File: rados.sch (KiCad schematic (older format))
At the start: 1 part

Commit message: More routing
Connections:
- net labels added: AUX-1, AUX-2, AUX-3, AUX-4, LCD-D4, LCD-D5, LCD-D6, LCD-D7, Probe
- net labels removed: LCD-4, LCD-5, LCD-6, LCD-7
- wire segments 66 -> 75
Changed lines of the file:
@@
 Text GLabel 5100 2800 2    47   Output ~ 0
 HP-FET2
-Text GLabel 5100 2700 2    47   Output ~ 0
+Text GLabel 5100 3400 2    47   Output ~ 0
 HP-FET3
+Text GLabel 5125 3700 2    47   Output ~ 0
+MP-FET1
+Text GLabel 5125 3800 2    47   Output ~ 0
+LP-FET1
 Text GLabel 5125 3900 2    47   Output ~ 0
-MP-FET1
-Text GLabel 5125 4100 2    47   Output ~ 0
-LP-FET1
-Text GLabel 5125 4000 2    47   Output ~ 0
 LP-FET2
 Wire Wire Line
@@
 	5000 2500 5100 2500
 Wire Wire Line
-	5000 2700 5100 2700
+	5000 3400 5100 3400
 Wire Wire Line
 	5100 2800 5000 2800
@@
 Text GLabel 5100 2100 2    47   Output ~ 0
 Z-EN
-Text GLabel 5125 3800 2    47   Output ~ 0
+Text GLabel 5100 3200 2    47   Output ~ 0
 Y-DIR
-Text GLabel 5125 3400 2    47   Output ~ 0
+Text GLabel 5100 3300 2    47   Output ~ 0
 Y-STEP
 Text GLabel 5125 4200 2    47   BiDi ~ 0
@@
 Wire Wire Line
 	5000 4625 5000 4725
-Text GLabel 5125 5050 2    47   Output ~ 0
+Text GLabel 5100 3100 2    47   Output ~ 0
 Y-EN
-Text GLabel 5125 5150 2    47   Output ~ 0
+Text GLabel 5125 4100 2    47   Output ~ 0
 X-DIR
-Text GLabel 5125 5250 2    47   Output ~ 0
+Text GLabel 5125 4000 2    47   Output ~ 0
 X-STEP
-Text GLabel 5125 5450 2    47   Output ~ 0
+Text GLabel 3000 6400 0    47   Output ~ 0
 X-EN
-Text GLabel 5125 5650 2    47   Input ~ 0
+Text GLabel 5125 5050 2    47   Input ~ 0
 X-
-Text GLabel 5125 5900 2    47   Input ~ 0
+Text GLabel 5125 5250 2    47   Input ~ 0
 Y-
-Text GLabel 5125 6100 2    47   Input ~ 0
+Text GLabel 5125 5450 2    47   Input ~ 0
 Z-
-Text GLabel 5125 6300 2    47   Input ~ 0
+Text GLabel 5125 5150 2    47   Input ~ 0
 X+
-Text GLabel 5125 6500 2    47   Input ~ 0
+Text GLabel 5125 5350 2    47   Input ~ 0
 Y+
-Text GLabel 3000 6600 0    47   Input ~ 0
+Text GLabel 5125 5550 2    47   Input ~ 0
 Z+
 Wire Wire Line
-	5000 5050 5125 5050
+	5125 5050 5000 5050
+Wire Wire Line
+	5000 5250 5125 5250
+Wire Wire Line
+	5000 5450 5125 5450
 Wire Wire Line
 	5125 5150 5000 5150
 Wire Wire Line
-	5000 5250 5125 5250
-Wire Wire Line
-	5000 5450 5125 5450
+	5000 5550 5125 5550
+Wire Wire Line
+	5125 6000 5000 6000
+Wire Wire Line
+	5000 5350 5125 5350
 Wire Wire Line
 	5125 5650 5000 5650
 Wire Wire Line
-	5000 5900 5125 5900
-Wire Wire Line
-	5125 6100 5000 6100
-Wire Wire Line
-	5000 6300 5125 6300
-Wire Wire Line
-	5125 6500 5000 6500
-Wire Wire Line
-	3000 6600 3100 6600
-Text GLabel 3000 6150 0    47   BiDi ~ 0
+	5125 6200 5000 6200
+Text GLabel 3000 6600 0    47   BiDi ~ 0
 LCD-RS
-Text GLabel 3000 6050 0    47   BiDi ~ 0
+Text GLabel 5125 6500 2    47   BiDi ~ 0
 LCD-E
-Text GLabel 3000 5950 0    47   BiDi ~ 0
-LCD-4
-Text GLabel 3000 5850 0    47   BiDi ~ 0
-LCD-5
-Text GLabel 3000 5750 0    47   BiDi ~ 0
-LCD-6
-Text GLabel 3000 5650 0    47   BiDi ~ 0
-LCD-7
-Text GLabel 3000 5550 0    47   BiDi ~ 0
+Text GLabel 5125 6200 2    47   BiDi ~ 0
+LCD-D4
+Text GLabel 5125 6600 2    47   BiDi ~ 0
+LCD-D5
+Text GLabel 5125 6400 2    47   BiDi ~ 0
+LCD-D6
+Text GLabel 5125 6300 2    47   BiDi ~ 0
+LCD-D7
+Text GLabel 2975 5550 0    47   BiDi ~ 0
 ENC-SW
-Text GLabel 3000 5300 0    47   BiDi ~ 0
+Text GLabel 3000 6500 0    47   BiDi ~ 0
 ENC-B
-Text GLabel 3000 5100 0    47   BiDi ~ 0
+Text GLabel 3000 6300 0    47   BiDi ~ 0
 ENC-A
 Wire Wire Line
-	3000 6150 3100 6150
-Wire Wire Line
-	3100 6050 3000 6050
-Wire Wire Line
-	3000 5950 3100 5950
-Wire Wire Line
-	3100 5850 3000 5850
-Wire Wire Line
-	3000 5750 3100 5750
-Wire Wire Line
-	3100 5650 3000 5650
-Wire Wire Line
-	3000 5550 3100 5550
+	2975 5550 3100 5550
 Wire Wire Line
 	3000 5300 3100 5300
 Wire Wire Line
 	3100 5100 3000 5100
-Text GLabel 3000 5450 0    47   Output ~ 0
+Text GLabel 2975 6150 0    47   Output ~ 0
 E3-EN
-Text GLabel 3000 5200 0    47   Output ~ 0
+Text GLabel 2975 5950 0    47   Output ~ 0
 E3-STEP
-Text GLabel 3000 5000 0    47   Output ~ 0
+Text GLabel 2975 5750 0    47   Output ~ 0
 E3-DIR
 Wire Wire Line
@@
 Wire Wire Line
 	3100 4625 3100 4850
-Text GLabel 3000 4000 0    47   Output ~ 0
+Text GLabel 2975 3300 0    47   Output ~ 0
 E2-STEP
-Text GLabel 3000 3400 0    47   Output ~ 0
+Text GLabel 2975 3400 0    47   Output ~ 0
 E2-EN
-Text GLabel 3000 3900 0    47   Output ~ 0
+Text GLabel 2975 3200 0    47   Output ~ 0
 E2-DIR
 Wire Wire Line
-	3000 3400 3100 3400
+	2975 3400 3100 3400
 Wire Wire Line
 	3100 4000 3000 4000
 Wire Wire Line
 	3000 3900 3100 3900
-Text GLabel 3000 3600 0    47   Output ~ 0
+Text GLabel 2975 3000 0    47   Output ~ 0
 E1-STEP
-Text GLabel 3000 3800 0    47   Output ~ 0
+Text GLabel 2975 3100 0    47   Output ~ 0
 E1-EN
-Text GLabel 3000 3500 0    47   Output ~ 0
+Text GLabel 2975 2900 0    47   Output ~ 0
 E1-DIR
 Wire Wire Line
@@
 Wire Wire Line
 	3000 2200 3100 2200
-Text GLabel 3000 4500 0    47   Input ~ 0
+Text GLabel 3000 4100 0    47   Input ~ 0
 T0
-Text GLabel 3000 4400 0    47   Input ~ 0
+Text GLabel 3000 4200 0    47   Input ~ 0
 T1
 Text GLabel 3000 4300 0    47   Input ~ 0
 T2
-Text GLabel 3000 4200 0    47   Input ~ 0
+Text GLabel 3000 4400 0    47   Input ~ 0
 T3
-Text GLabel 3000 4100 0    47   Input ~ 0
+Text GLabel 3000 4500 0    47   Input ~ 0
 T4
 Wire Wire Line
@@
 Wire Wire Line
 	3000 4100 3100 4100
-Text GLabel 3000 6300 0    47   Input ~ 0
+Text GLabel 5125 5750 2    47   Input ~ 0
 STATUS-LED
 Wire Wire Line
@@
 	5000 4000 5125 4000
 Wire Wire Line
-	5125 3400 5000 3400
+	5100 3300 5000 3300
+Text GLabel 5125 5650 2    47   Input ~ 0
+Probe
+Wire Wire Line
+	5000 6400 5125 6400
+Wire Wire Line
+	5000 6500 5125 6500
+Wire Wire Line
+	3000 6400 3100 6400
+Wire Wire Line
+	3000 6600 3100 6600
+Wire Wire Line
+	5125 6600 5000 6600
+Wire Wire Line
+	5125 6300 5000 6300
+Text GLabel 3000 3600 0    47   BiDi ~ 0
+AUX-1
+Text GLabel 3000 3800 0    47   BiDi ~ 0
+AUX-2
+Text GLabel 3000 3900 0    47   BiDi ~ 0
+AUX-3
+Text GLabel 3000 4000 0    47   BiDi ~ 0
+AUX-4
+Wire Wire Line
+	2975 2900 3100 2900
+Wire Wire Line
+	3100 3000 2975 3000
+Wire Wire Line
+	2975 3100 3100 3100
+Wire Wire Line
+	2975 3200 3100 3200
+Wire Wire Line
+	3100 3300 2975 3300
+Wire Wire Line
+	3000 6500 3100 6500
+Wire Wire Line
+	3100 6150 2975 6150
+Wire Wire Line
+	5125 5750 5000 5750
+Wire Wire Line
+	2975 5750 3100 5750
+Wire Wire Line
+	2975 5950 3100 5950
 $EndSCHEMATC

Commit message: Routing almost finished
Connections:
- wire segments 75 -> 77
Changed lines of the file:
@@
 Text GLabel 5100 2000 2    47   Output ~ 0
 HB-FET
-Text GLabel 5100 2500 2    47   Output ~ 0
+Text GLabel 5100 2700 2    47   Output ~ 0
 HP-FET1
 Text GLabel 5100 2800 2    47   Output ~ 0
@@
 Text GLabel 5100 2200 2    47   Output ~ 0
 Z-DIR
-Text GLabel 5100 2400 2    47   Output ~ 0
+Text GLabel 5100 2500 2    47   Output ~ 0
 Z-STEP
 Wire Wire Line
@@
 Text GLabel 5100 3200 2    47   Output ~ 0
 Y-DIR
-Text GLabel 5100 3300 2    47   Output ~ 0
+Text GLabel 5100 3100 2    47   Output ~ 0
 Y-STEP
 Text GLabel 5125 4200 2    47   BiDi ~ 0
@@
 Wire Wire Line
 	5000 4625 5000 4725
-Text GLabel 5100 3100 2    47   Output ~ 0
+Text GLabel 5100 3300 2    47   Output ~ 0
 Y-EN
 Text GLabel 5125 4100 2    47   Output ~ 0
@@
 Text GLabel 5125 6300 2    47   BiDi ~ 0
 LCD-D7
-Text GLabel 2975 5550 0    47   BiDi ~ 0
+Text GLabel 5100 2400 2    47   BiDi ~ 0
 ENC-SW
 Text GLabel 3000 6500 0    47   BiDi ~ 0
@@
 Wire Wire Line
 	3100 5100 3000 5100
-Text GLabel 2975 6150 0    47   Output ~ 0
+Text GLabel 2975 5950 0    47   Output ~ 0
 E3-EN
-Text GLabel 2975 5950 0    47   Output ~ 0
+Text GLabel 2975 5850 0    47   Output ~ 0
 E3-STEP
 Text GLabel 2975 5750 0    47   Output ~ 0
@@
 Wire Wire Line
 	2975 5950 3100 5950
+Wire Wire Line
+	2975 5850 3100 5850
+Wire Wire Line
+	5100 2700 5000 2700
 $EndSCHEMATC

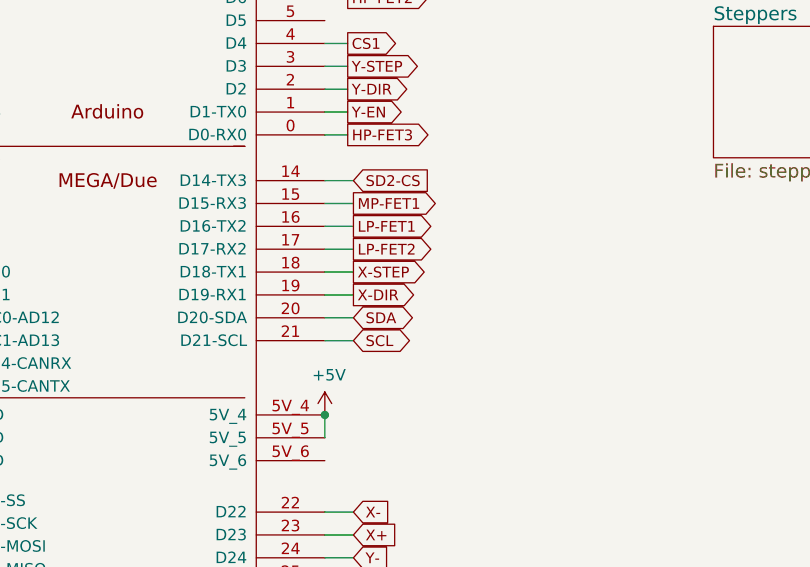
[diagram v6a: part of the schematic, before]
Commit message: - added wifi esp8266 - switched caps to smd - fixed dual transistor pinout bug
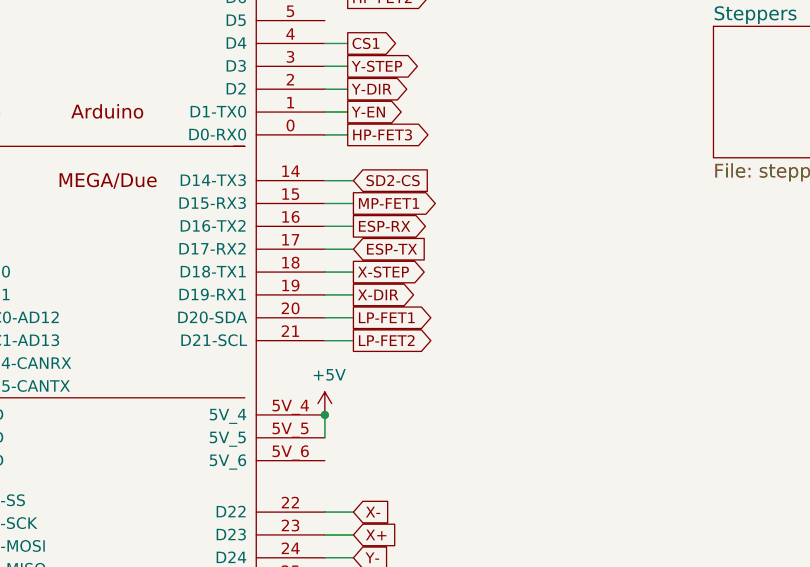
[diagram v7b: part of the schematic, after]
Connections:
- net labels added: ESP-RX, ESP-TX
- net labels removed: SCL, SDA
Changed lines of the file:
@@
 EESchema Schematic File Version 2
+LIBS:rados-rescue
+LIBS:import-transistors
+LIBS:import-regulators
+LIBS:import-opamps
+LIBS:import-diodes
 LIBS:led_reverse
 LIBS:arduino_shieldsNCL
 LIBS:otheruse_transistors
 LIBS:custom_power
-LIBS:import_resistors
-LIBS:import_regulators
-LIBS:import_transistors
-LIBS:import_diodes
+LIBS:import-misc
+LIBS:armin_misc
 LIBS:power
 LIBS:device
 LIBS:transistors
 LIBS:conn
-LIBS:import_misc
 LIBS:linear
 LIBS:regul
@@
 LIBS:valves
 LIBS:arduino
+LIBS:ESP8266
 LIBS:rados-cache
 EELAYER 25 0
@@
 Text GLabel 5125 3700 2    47   Output ~ 0
 MP-FET1
-Text GLabel 5125 3800 2    47   Output ~ 0
+Text GLabel 5125 4200 2    47   Output ~ 0
 LP-FET1
-Text GLabel 5125 3900 2    47   Output ~ 0
+Text GLabel 5125 4300 2    47   Output ~ 0
 LP-FET2
 Wire Wire Line
@@
 Text GLabel 5100 3100 2    47   Output ~ 0
 Y-STEP
-Text GLabel 5125 4200 2    47   BiDi ~ 0
-SDA
-Text GLabel 5125 4300 2    47   BiDi ~ 0
-SCL
 $Comp
 L +5V #PWR04
@@
 Wire Wire Line
 	5100 2700 5000 2700
+Text GLabel 5125 3800 2    47   Output ~ 0
+ESP-RX
+Text GLabel 5125 3900 2    47   Input ~ 0
+ESP-TX
 $EndSCHEMATC

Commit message: Routing
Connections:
- net labels added: PROBE
- net labels removed: Probe
- wire segments 77 -> 79
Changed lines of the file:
@@
 Text GLabel 5125 4000 2    47   Output ~ 0
 X-STEP
-Text GLabel 3000 6400 0    47   Output ~ 0
+Text GLabel 2975 6150 0    47   Output ~ 0
 X-EN
-Text GLabel 5125 5050 2    47   Input ~ 0
+Text GLabel 5125 6400 2    47   Input ~ 0
 X-
-Text GLabel 5125 5250 2    47   Input ~ 0
+Text GLabel 5125 6600 2    47   Input ~ 0
 Y-
-Text GLabel 5125 5450 2    47   Input ~ 0
+Text GLabel 3000 6500 0    47   Input ~ 0
 Z-
-Text GLabel 5125 5150 2    47   Input ~ 0
+Text GLabel 5125 6500 2    47   Input ~ 0
 X+
-Text GLabel 5125 5350 2    47   Input ~ 0
+Text GLabel 3000 6600 0    47   Input ~ 0
 Y+
-Text GLabel 5125 5550 2    47   Input ~ 0
+Text GLabel 3000 6400 0    47   Input ~ 0
 Z+
 Wire Wire Line
@@
 Wire Wire Line
 	5125 6200 5000 6200
-Text GLabel 3000 6600 0    47   BiDi ~ 0
+Text GLabel 5125 5900 2    47   BiDi ~ 0
 LCD-RS
-Text GLabel 5125 6500 2    47   BiDi ~ 0
+Text GLabel 5125 6100 2    47   BiDi ~ 0
 LCD-E
+Text GLabel 5125 6300 2    47   BiDi ~ 0
+LCD-D4
+Text GLabel 5125 5750 2    47   BiDi ~ 0
+LCD-D5
+Text GLabel 5125 6000 2    47   BiDi ~ 0
+LCD-D6
 Text GLabel 5125 6200 2    47   BiDi ~ 0
-LCD-D4
-Text GLabel 5125 6600 2    47   BiDi ~ 0
-LCD-D5
-Text GLabel 5125 6400 2    47   BiDi ~ 0
-LCD-D6
-Text GLabel 5125 6300 2    47   BiDi ~ 0
 LCD-D7
 Text GLabel 5100 2400 2    47   BiDi ~ 0
 ENC-SW
-Text GLabel 3000 6500 0    47   BiDi ~ 0
+Text GLabel 5125 5650 2    47   BiDi ~ 0
 ENC-B
-Text GLabel 3000 6300 0    47   BiDi ~ 0
+Text GLabel 5125 5550 2    47   BiDi ~ 0
 ENC-A
 Wire Wire Line
@@
 Wire Wire Line
 	3000 4100 3100 4100
-Text GLabel 5125 5750 2    47   Input ~ 0
+Text GLabel 5125 5350 2    47   Input ~ 0
 STATUS-LED
 Wire Wire Line
@@
 Wire Wire Line
 	5100 3300 5000 3300
-Text GLabel 5125 5650 2    47   Input ~ 0
-Probe
+Text GLabel 3000 6300 0    47   Input ~ 0
+PROBE
 Wire Wire Line
 	5000 6400 5125 6400
@@
 Text GLabel 5125 3900 2    47   Input ~ 0
 ESP-TX
+Wire Wire Line
+	5000 6100 5125 6100
+Wire Wire Line
+	5125 5900 5000 5900
 $EndSCHEMATC
